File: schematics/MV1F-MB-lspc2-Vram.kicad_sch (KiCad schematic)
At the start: 33 parts, among them J10 NO, J2 NO, J6 NO

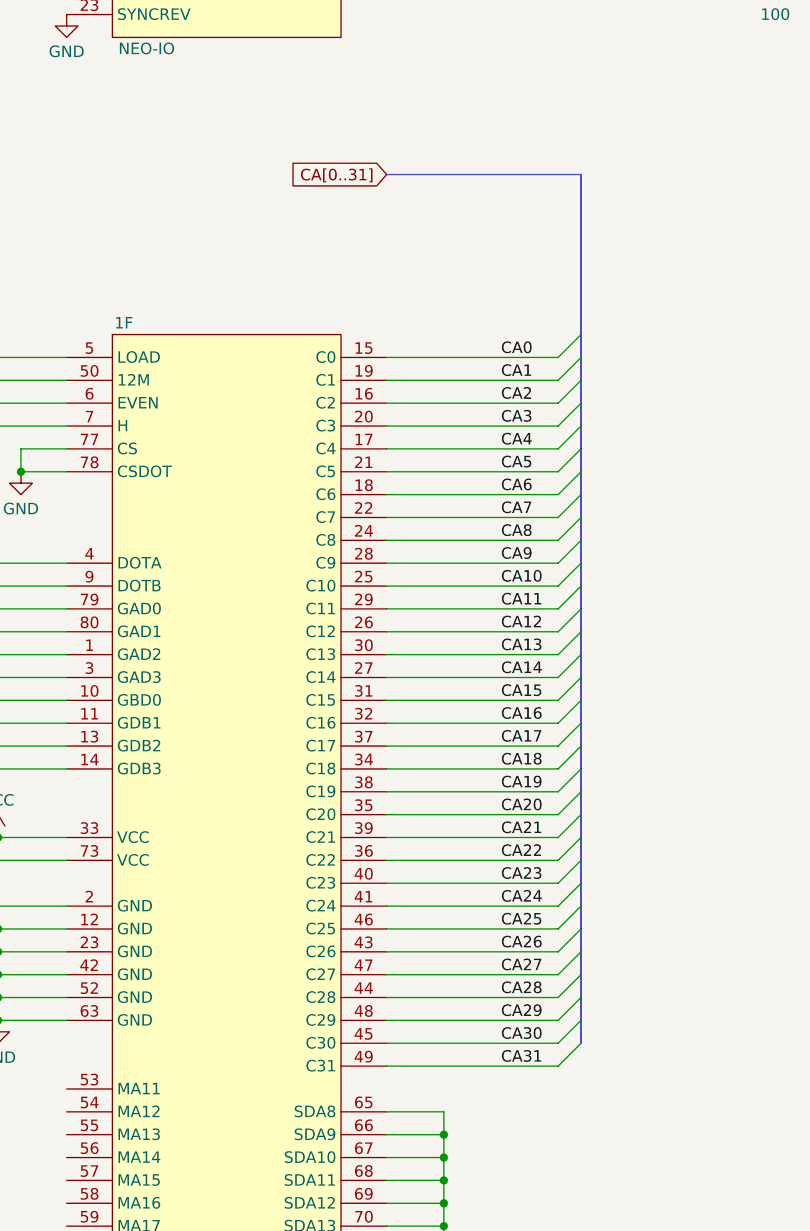
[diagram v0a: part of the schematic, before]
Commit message: complete DaughterBoard
rename sub files
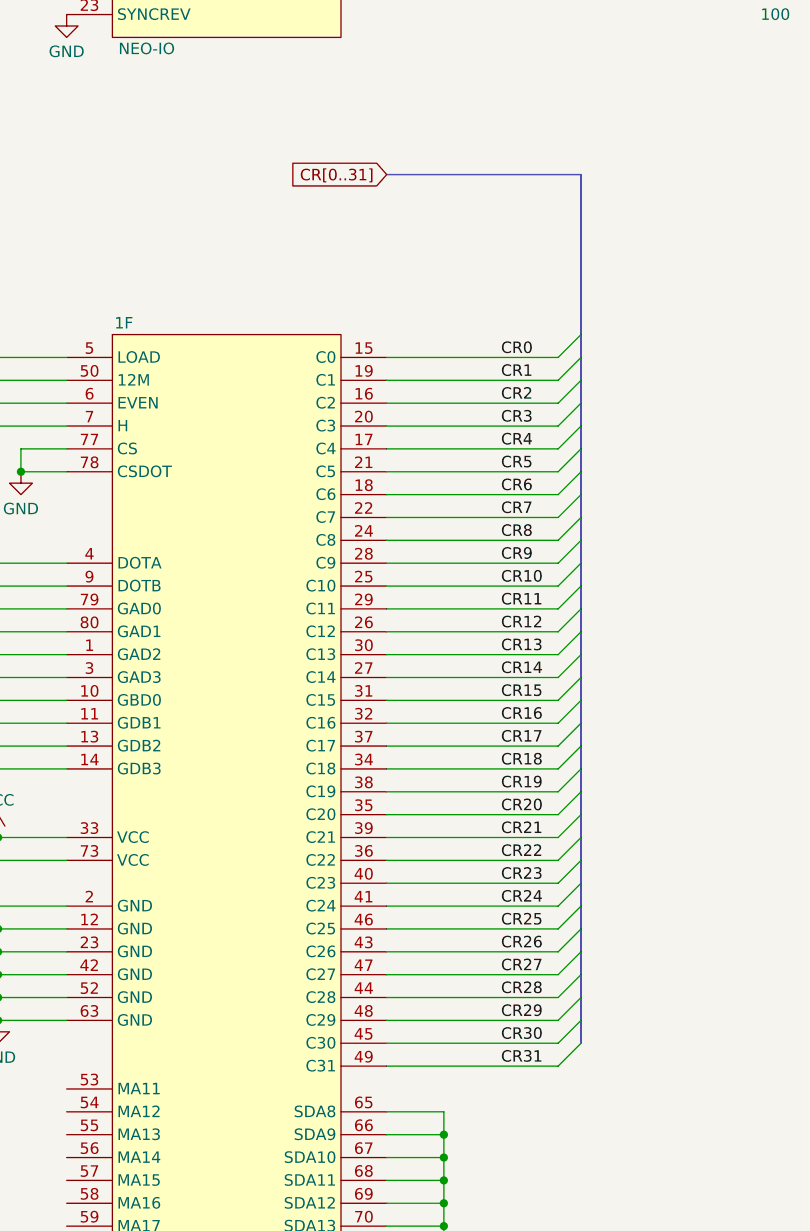
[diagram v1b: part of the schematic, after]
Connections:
- net CA4: no longer 1F.17 (C4)
- net CA0 renamed CR0
- net CA1 renamed CR1
- net CA10 renamed CR10
- net CA11 renamed CR11
- net CA12 renamed CR12
- net CA13 renamed CR13
- net CA14 renamed CR14
- net CA15 renamed CR15
- net CA16 renamed CR16
- net CA17 renamed CR17
- net CA18 renamed CR18
- net CA19 renamed CR19
- net CA2 renamed CR2
- net CA20 renamed CR20
- net CA21 renamed CR21
- net CA22 renamed CR22
- net CA23 renamed CR23
- net CA24 renamed CR24
- net CA25 renamed CR25
- net CA26 renamed CR26
- net CA27 renamed CR27
- net CA28 renamed CR28
- net CA29 renamed CR29
- net CA3 renamed CR3
- net CA30 renamed CR30
- net CA31 renamed CR31
- net CA5 renamed CR5
- net CA6 renamed CR6
- net CA7 renamed CR7
- net CA8 renamed CR8
- net CA9 renamed CR9
- new net CR4: 1F.17 (C4)
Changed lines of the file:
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@@
     (effects (font (size 1.27 1.27)) (justify left bottom))
   )
-  (label "CA20" (at 410.21 219.71 0) (fields_autoplaced)
+  (label "CR20" (at 410.21 219.71 0) (fields_autoplaced)
     (effects (font (size 1.27 1.27)) (justify left bottom))
   )
@@
     (effects (font (size 1.27 1.27)) (justify left bottom))
   )
-  (label "CA29" (at 410.21 242.57 0) (fields_autoplaced)
+  (label "CR29" (at 410.21 242.57 0) (fields_autoplaced)
     (effects (font (size 1.27 1.27)) (justify left bottom))
   )
@@
     (effects (font (size 1.27 1.27)) (justify left bottom))
   )
-  (label "CA5" (at 410.21 181.61 0) (fields_autoplaced)
+  (label "CR5" (at 410.21 181.61 0) (fields_autoplaced)
     (effects (font (size 1.27 1.27)) (justify left bottom))
   )
@@
     (effects (font (size 1.27 1.27)) (justify left bottom))
   )
-  (label "CA22" (at 410.21 224.79 0) (fields_autoplaced)
+  (label "CR22" (at 410.21 224.79 0) (fields_autoplaced)
     (effects (font (size 1.27 1.27)) (justify left bottom))
   )
@@
     (effects (font (size 1.27 1.27)) (justify left bottom))
   )
-  (label "CA25" (at 410.21 232.41 0) (fields_autoplaced)
+  (label "CR25" (at 410.21 232.41 0) (fields_autoplaced)
     (effects (font (size 1.27 1.27)) (justify left bottom))
   )
@@
     (effects (font (size 1.27 1.27)) (justify right bottom))
   )
-  (label "CA27" (at 410.21 237.49 0) (fields_autoplaced)
+  (label "CR27" (at 410.21 237.49 0) (fields_autoplaced)
     (effects (font (size 1.27 1.27)) (justify left bottom))
   )
@@
     (effects (font (size 1.27 1.27)) (justify left bottom))
   )
-  (label "CA7" (at 410.21 186.69 0) (fields_autoplaced)
+  (label "CR7" (at 410.21 186.69 0) (fields_autoplaced)
     (effects (font (size 1.27 1.27)) (justify left bottom))
   )
@@
     (effects (font (size 1.27 1.27)) (justify left bottom))
   )
-  (label "CA18" (at 410.21 214.63 0) (fields_autoplaced)
+  (label "CR18" (at 410.21 214.63 0) (fields_autoplaced)
     (effects (font (size 1.27 1.27)) (justify left bottom))
   )
@@
     (effects (font (size 1.27 1.27)) (justify left bottom))
   )
-  (label "CA12" (at 410.21 199.39 0) (fields_autoplaced)
+  (label "CR12" (at 410.21 199.39 0) (fields_autoplaced)
     (effects (font (size 1.27 1.27)) (justify left bottom))
   )
@@
     (effects (font (size 1.27 1.27)) (justify left bottom))
   )
-  (label "CA0" (at 410.21 168.91 0) (fields_autoplaced)
-    (effects (font (size 1.27 1.27)) (justify left bottom))
-  )
-  (label "CA3" (at 410.21 176.53 0) (fields_autoplaced)
+  (label "CR0" (at 410.21 168.91 0) (fields_autoplaced)
+    (effects (font (size 1.27 1.27)) (justify left bottom))
+  )
+  (label "CR3" (at 410.21 176.53 0) (fields_autoplaced)
     (effects (font (size 1.27 1.27)) (justify left bottom))
   )
@@
     (effects (font (size 1.27 1.27)) (justify left bottom))
   )
-  (label "CA19" (at 410.21 217.17 0) (fields_autoplaced)
+  (label "CR19" (at 410.21 217.17 0) (fields_autoplaced)
     (effects (font (size 1.27 1.27)) (justify left bottom))
   )
@@
     (effects (font (size 1.27 1.27)) (justify left bottom))
   )
-  (label "CA24" (at 410.21 229.87 0) (fields_autoplaced)
+  (label "CR24" (at 410.21 229.87 0) (fields_autoplaced)
     (effects (font (size 1.27 1.27)) (justify left bottom))
   )
@@
     (effects (font (size 1.27 1.27)) (justify left bottom))
   )
-  (label "CA4" (at 410.21 179.07 0) (fields_autoplaced)
+  (label "CR4" (at 410.21 179.07 0) (fields_autoplaced)
     (effects (font (size 1.27 1.27)) (justify left bottom))
   )
@@
     (effects (font (size 1.27 1.27)) (justify left bottom))
   )
-  (label "CA31" (at 410.21 247.65 0) (fields_autoplaced)
-    (effects (font (size 1.27 1.27)) (justify left bottom))
-  )
-  (label "CA21" (at 410.21 222.25 0) (fields_autoplaced)
+  (label "CR31" (at 410.21 247.65 0) (fields_autoplaced)
+    (effects (font (size 1.27 1.27)) (justify left bottom))
+  )
+  (label "CR21" (at 410.21 222.25 0) (fields_autoplaced)
     (effects (font (size 1.27 1.27)) (justify left bottom))
   )
@@
     (effects (font (size 1.27 1.27)) (justify left bottom))
   )
-  (label "CA28" (at 410.21 240.03 0) (fields_autoplaced)
+  (label "CR28" (at 410.21 240.03 0) (fields_autoplaced)
     (effects (font (size 1.27 1.27)) (justify left bottom))
   )
@@
     (effects (font (size 1.27 1.27)) (justify left bottom))
   )
-  (label "CA9" (at 410.21 191.77 0) (fields_autoplaced)
+  (label "CR9" (at 410.21 191.77 0) (fields_autoplaced)
     (effects (font (size 1.27 1.27)) (justify left bottom))
   )
@@
     (effects (font (size 1.27 1.27)) (justify left bottom))
   )
-  (label "CA23" (at 410.21 227.33 0) (fields_autoplaced)
+  (label "CR23" (at 410.21 227.33 0) (fields_autoplaced)
     (effects (font (size 1.27 1.27)) (justify left bottom))
   )
@@
     (effects (font (size 1.27 1.27)) (justify left bottom))
   )
-  (label "CA16" (at 410.21 209.55 0) (fields_autoplaced)
+  (label "CR16" (at 410.21 209.55 0) (fields_autoplaced)
     (effects (font (size 1.27 1.27)) (justify left bottom))
   )
@@
     (effects (font (size 1.27 1.27)) (justify left bottom))
   )
-  (label "CA26" (at 410.21 234.95 0) (fields_autoplaced)
+  (label "CR26" (at 410.21 234.95 0) (fields_autoplaced)
     (effects (font (size 1.27 1.27)) (justify left bottom))
   )
@@
     (effects (font (size 1.27 1.27)) (justify left bottom))
   )
-  (label "CA2" (at 410.21 173.99 0) (fields_autoplaced)
+  (label "CR2" (at 410.21 173.99 0) (fields_autoplaced)
     (effects (font (size 1.27 1.27)) (justify left bottom))
   )
@@
     (effects (font (size 1.27 1.27)) (justify left bottom))
   )
-  (label "CA13" (at 410.21 201.93 0) (fields_autoplaced)
+  (label "CR13" (at 410.21 201.93 0) (fields_autoplaced)
     (effects (font (size 1.27 1.27)) (justify left bottom))
   )
@@
     (effects (font (size 1.27 1.27)) (justify left bottom))
   )
-  (label "CA10" (at 410.21 194.31 0) (fields_autoplaced)
+  (label "CR10" (at 410.21 194.31 0) (fields_autoplaced)
     (effects (font (size 1.27 1.27)) (justify left bottom))
   )
@@
     (effects (font (size 1.27 1.27)) (justify left bottom))
   )
-  (label "CA8" (at 410.21 189.23 0) (fields_autoplaced)
+  (label "CR8" (at 410.21 189.23 0) (fields_autoplaced)
     (effects (font (size 1.27 1.27)) (justify left bottom))
   )
@@
     (effects (font (size 1.27 1.27)) (justify left bottom))
   )
-  (label "CA15" (at 410.21 207.01 0) (fields_autoplaced)
+  (label "CR15" (at 410.21 207.01 0) (fields_autoplaced)
     (effects (font (size 1.27 1.27)) (justify left bottom))
   )
@@
     (effects (font (size 1.27 1.27)) (justify left bottom))
   )
-  (label "CA11" (at 410.21 196.85 0) (fields_autoplaced)
+  (label "CR11" (at 410.21 196.85 0) (fields_autoplaced)
     (effects (font (size 1.27 1.27)) (justify left bottom))
   )
@@
     (effects (font (size 1.27 1.27)) (justify left bottom))
   )
-  (label "CA6" (at 410.21 184.15 0) (fields_autoplaced)
+  (label "CR6" (at 410.21 184.15 0) (fields_autoplaced)
     (effects (font (size 1.27 1.27)) (justify left bottom))
   )
@@
     (effects (font (size 1.27 1.27)) (justify left bottom))
   )
-  (label "CA17" (at 410.21 212.09 0) (fields_autoplaced)
+  (label "CR17" (at 410.21 212.09 0) (fields_autoplaced)
     (effects (font (size 1.27 1.27)) (justify left bottom))
   )
@@
     (effects (font (size 1.27 1.27)) (justify left bottom))
   )
-  (label "CA1" (at 410.21 171.45 0) (fields_autoplaced)
+  (label "CR1" (at 410.21 171.45 0) (fields_autoplaced)
     (effects (font (size 1.27 1.27)) (justify left bottom))
   )
@@
     (effects (font (size 1.27 1.27)) (justify left bottom))
   )
-  (label "CA30" (at 410.21 245.11 0) (fields_autoplaced)
+  (label "CR30" (at 410.21 245.11 0) (fields_autoplaced)
     (effects (font (size 1.27 1.27)) (justify left bottom))
   )
@@
     (effects (font (size 1.27 1.27)) (justify left bottom))
   )
-  (label "CA14" (at 410.21 204.47 0) (fields_autoplaced)
+  (label "CR14" (at 410.21 204.47 0) (fields_autoplaced)
     (effects (font (size 1.27 1.27)) (justify left bottom))
   )
@@
     )
   )
-  (global_label "CA[0..31]" (shape input) (at 397.51 148.59 180) (fields_autoplaced)
+  (global_label "CR[0..31]" (shape input) (at 397.51 148.59 180) (fields_autoplaced)
     (effects (font (size 1.27 1.27)) (justify right))
     (property "Intersheetrefs" "${INTERSHEET_REFS}" (at 385.6347 148.59 0)

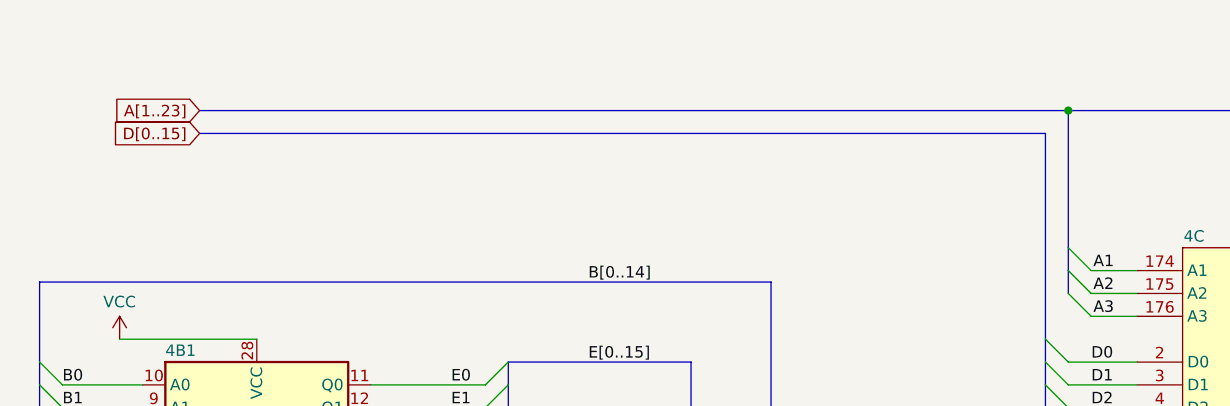
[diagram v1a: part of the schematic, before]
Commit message: Typo... and orphan labels remove
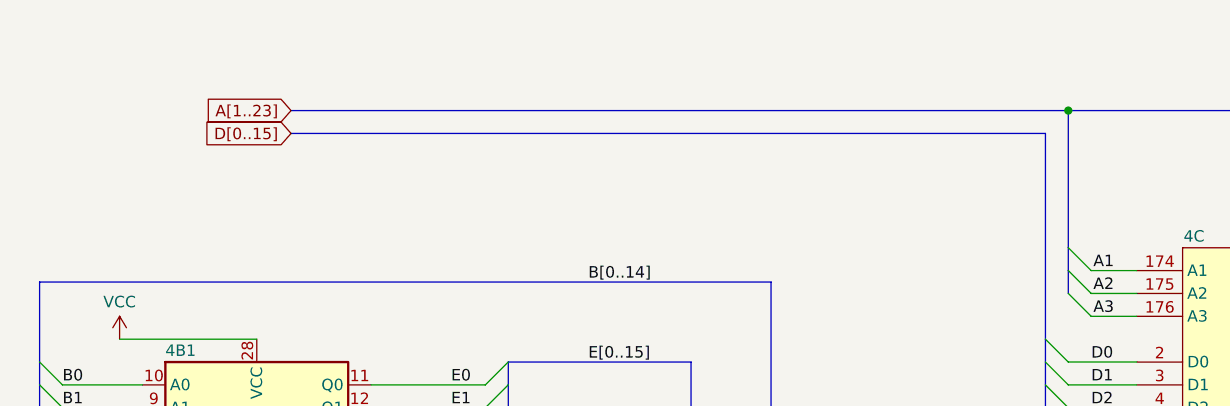
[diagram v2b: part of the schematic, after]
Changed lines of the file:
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@@
     (stroke (width 0) (type default))
   )
-  (bus (pts (xy 39.37 30.48) (xy 133.35 30.48))
+  (bus (pts (xy 49.53 30.48) (xy 133.35 30.48))
     (stroke (width 0) (type default))
   )
@@
     (stroke (width 0) (type default))
   )
-  (bus (pts (xy 39.37 27.94) (xy 135.89 27.94))
+  (bus (pts (xy 49.53 27.94) (xy 135.89 27.94))
     (stroke (width 0) (type default))
   )
@@
     )
   )
-  (global_label "A[1..23]" (shape input) (at 39.37 27.94 180) (fields_autoplaced)
-    (effects (font (size 1.27 1.27)) (justify right))
-    (property "Intersheetrefs" "${INTERSHEET_REFS}" (at 28.7647 27.94 0)
+  (global_label "A[1..23]" (shape input) (at 49.53 27.94 180) (fields_autoplaced)
+    (effects (font (size 1.27 1.27)) (justify right))
+    (property "Intersheetrefs" "${INTERSHEET_REFS}" (at 38.9247 27.94 0)
       (effects (font (size 1.27 1.27)) (justify right))
     )
@@
     )
   )
-  (global_label "D[0..15]" (shape input) (at 39.37 30.48 180) (fields_autoplaced)
-    (effects (font (size 1.27 1.27)) (justify right))
-    (property "Intersheetrefs" "${INTERSHEET_REFS}" (at 28.5833 30.48 0)
-      (effects (font (size 1.27 1.27)) (justify right))
-    )
+  (global_label "D[0..15]" (shape input) (at 49.53 30.48 180) (fields_autoplaced)
+    (effects (font (size 1.27 1.27)) (justify right))
+    (property "Intersheetrefs" "${INTERSHEET_REFS}" (at 38.7433 30.48 0)
+      (effects (font (size 1.27 1.27)) (justify right))
+    )
